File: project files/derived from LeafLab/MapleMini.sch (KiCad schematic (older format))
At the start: 40 parts, among them J1 USB_C, J2 Conn_ST_STDC14, J3 Left, J4 Right, Q1 BC817, Q2 BC817, SW1 Reset, SW2 Button, U1 STM32F103CBTx, U2 MCP1703A-3302_SOT23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

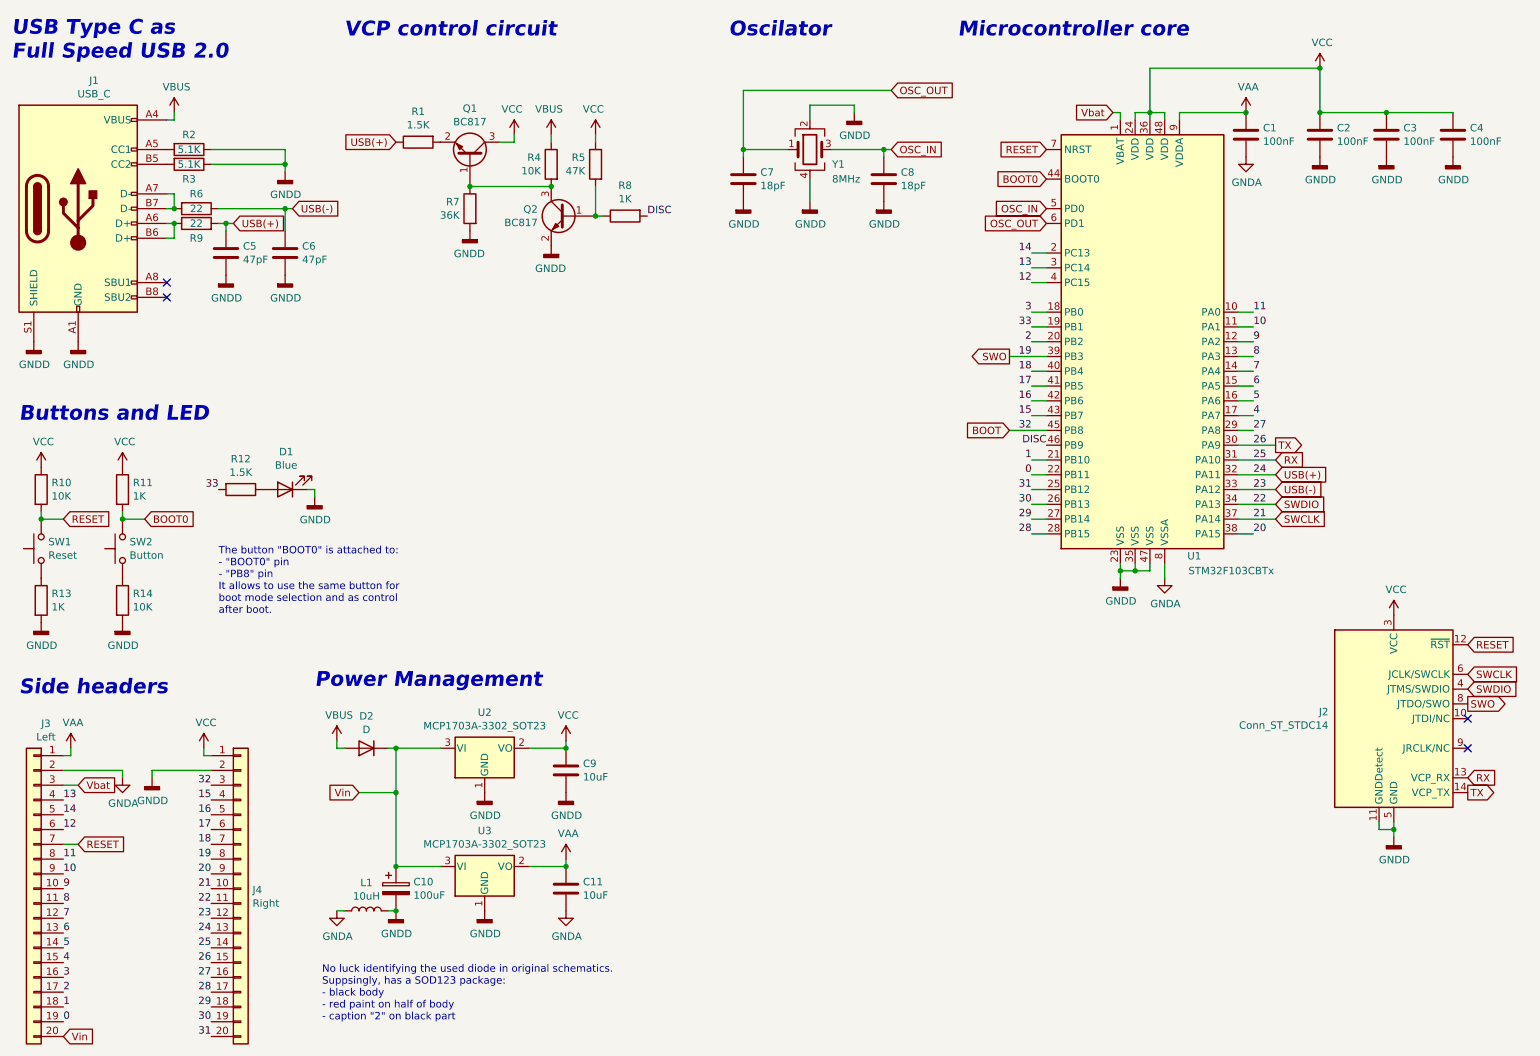
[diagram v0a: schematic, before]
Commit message: power nets renaming
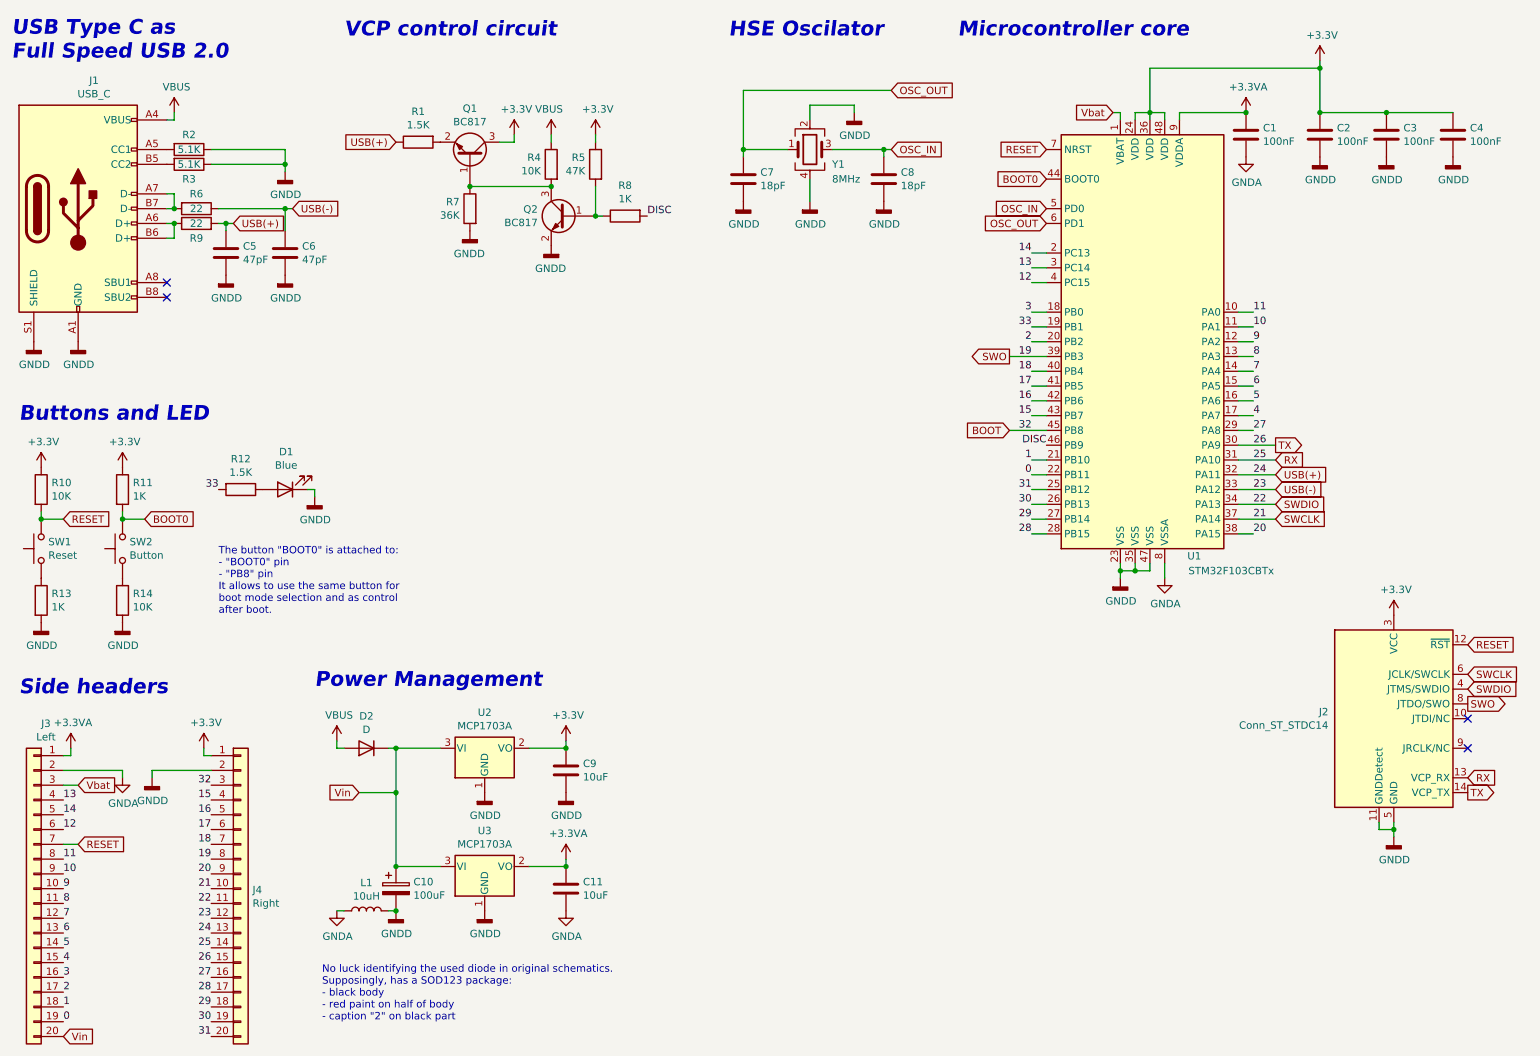
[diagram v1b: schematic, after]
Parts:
- U2, U3: value MCP1703A-3302_SOT23 -> MCP1703A
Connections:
- net VAA renamed +3.3VA
- net VCC renamed +3V3
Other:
- note added: "HSE Oscilator"
- note added: "No luck identifying the used diode in original schematics.\nSupposingly, has a SOD123 package:\n- black body\n- red paint on half of body\n- caption "2" on black part"
- note removed: "No luck identifying the used diode in original schematics.\nSuppsingly, has a SOD123 package:\n- black body\n- red paint on half of body\n- caption "2" on black part"
- note removed: "Oscilator"
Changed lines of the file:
@@
-$EndComp
-$Comp
-L power:VCC #PWR04
-U 1 1 5F576CBF
-P 4100 1500
-F 0 "#PWR04" H 4100 1350 50  0001 C CNN
-F 1 "VCC" H 4115 1673 50  0000 C CNN
-F 2 "" H 4100 1500 50  0001 C CNN
-F 3 "" H 4100 1500 50  0001 C CNN
-	1    4100 1500
-	-1   0    0    -1
 $EndComp
 $Comp
@@
 	-1   0    0    -1
 $EndComp
-$Comp
-L power:VCC #PWR06
-U 1 1 5F588E4C
-P 4650 1500
-F 0 "#PWR06" H 4650 1350 50  0001 C CNN
-F 1 "VCC" H 4665 1673 50  0000 C CNN
-F 2 "" H 4650 1500 50  0001 C CNN
-F 3 "" H 4650 1500 50  0001 C CNN
-	1    4650 1500
-	-1   0    0    -1
-$EndComp
 Wire Wire Line
 	3800 1850 4350 1850
@@
 P 3900 5650
 F 0 "U2" H 3900 5892 50  0000 C CNN
-F 1 "MCP1703A-3302_SOT23" H 3900 5801 50  0000 C CNN
+F 1 "MCP1703A" H 3900 5801 50  0000 C CNN
 F 2 "Package_TO_SOT_SMD:SOT-23" H 3900 5850 50  0001 C CNN
 F 3 "http://ww1.microchip.com/downloads/en/DeviceDoc/20005122B.pdf" H 3900 5600 50  0001 C CNN
@@
 P 3900 6450
 F 0 "U3" H 3900 6692 50  0000 C CNN
-F 1 "MCP1703A-3302_SOT23" H 3900 6601 50  0000 C CNN
+F 1 "MCP1703A" H 3900 6601 50  0000 C CNN
 F 2 "Package_TO_SOT_SMD:SOT-23" H 3900 6650 50  0001 C CNN
 F 3 "http://ww1.microchip.com/downloads/en/DeviceDoc/20005122B.pdf" H 3900 6400 50  0001 C CNN
@@
 $EndComp
 $Comp
-L power:VCC #PWR035
-U 1 1 5F59C36D
-P 4450 5600
-F 0 "#PWR035" H 4450 5450 50  0001 C CNN
-F 1 "VCC" H 4465 5773 50  0000 C CNN
-F 2 "" H 4450 5600 50  0001 C CNN
-F 3 "" H 4450 5600 50  0001 C CNN
-	1    4450 5600
-	1    0    0    -1
-$EndComp
-$Comp
 L power:GNDA #PWR023
 U 1 1 5F59D10D
@@
 F 3 "" H 8500 4500 50  0001 C CNN
 	1    8500 4500
-	1    0    0    -1
-$EndComp
-$Comp
-L power:VAA #PWR039
-U 1 1 5F59E88F
-P 4450 6400
-F 0 "#PWR039" H 4450 6250 50  0001 C CNN
-F 1 "VAA" H 4465 6573 50  0000 C CNN
-F 2 "" H 4450 6400 50  0001 C CNN
-F 3 "" H 4450 6400 50  0001 C CNN
-	1    4450 6400
 	1    0    0    -1
 $EndComp
@@
 $EndComp
 $Comp
-L power:VCC #PWR018
-U 1 1 5F5DF46D
-P 900 3750
-F 0 "#PWR018" H 900 3600 50  0001 C CNN
-F 1 "VCC" H 915 3923 50  0000 C CNN
-F 2 "" H 900 3750 50  0001 C CNN
-F 3 "" H 900 3750 50  0001 C CNN
-	1    900  3750
-	1    0    0    -1
-$EndComp
-$Comp
-L power:VCC #PWR019
-U 1 1 5F5E053F
-P 1450 3750
-F 0 "#PWR019" H 1450 3600 50  0001 C CNN
-F 1 "VCC" H 1465 3923 50  0000 C CNN
-F 2 "" H 1450 3750 50  0001 C CNN
-F 3 "" H 1450 3750 50  0001 C CNN
-	1    1450 3750
-	1    0    0    -1
-$EndComp
-$Comp
 L Device:R R10
 U 1 1 5F5E0C66
@@
 	8600 1350 8600 1400
 $Comp
-L power:VAA #PWR03
-U 1 1 5F61B614
-P 9050 1350
-F 0 "#PWR03" H 9050 1200 50  0001 C CNN
-F 1 "VAA" H 9065 1523 50  0000 C CNN
-F 2 "" H 9050 1350 50  0001 C CNN
-F 3 "" H 9050 1350 50  0001 C CNN
-	1    9050 1350
-	1    0    0    -1
-$EndComp
-Connection ~ 9050 1350
-$Comp
 L power:GNDD #PWR08
 U 1 1 5F61C6D4
@@
 	8400 1050 8400 1350
 Connection ~ 9550 1350
-$Comp
-L power:VCC #PWR01
-U 1 1 5F620163
-P 9550 1050
-F 0 "#PWR01" H 9550 900 50  0001 C CNN
-F 1 "VCC" H 9565 1223 50  0000 C CNN
-F 2 "" H 9550 1050 50  0001 C CNN
-F 3 "" H 9550 1050 50  0001 C CNN
-	1    9550 1050
-	1    0    0    -1
-$EndComp
-Connection ~ 9550 1050
 $Comp
 L Connector_Generic:Conn_01x20 J4
@@
 	1    850  6600
 	-1   0    0    -1
-$EndComp
-$Comp
-L power:VAA #PWR030
-U 1 1 5F62AD2E
-P 1100 5650
-F 0 "#PWR030" H 1100 5500 50  0001 C CNN
-F 1 "VAA" H 1115 5823 50  0000 C CNN
-F 2 "" H 1100 5650 50  0001 C CNN
-F 3 "" H 1100 5650 50  0001 C CNN
-	1    1100 5650
-	1    0    0    -1
 $EndComp
 $Comp
@@
 Wire Wire Line
 	1100 5700 1100 5650
-$Comp
-L power:VCC #PWR031
-U 1 1 5F63C308
-P 2000 5650
-F 0 "#PWR031" H 2000 5500 50  0001 C CNN
-F 1 "VCC" H 2015 5823 50  0000 C CNN
-F 2 "" H 2000 5650 50  0001 C CNN
-F 3 "" H 2000 5650 50  0001 C CNN
-	1    2000 5650
-	1    0    0    -1
-$EndComp
 $Comp
 L power:GNDD #PWR033
@@
 VCP control circuit
 Text Notes 5550 850  0    100  Italic 20
-Oscilator
+HSE Oscilator
 Text Notes 7100 850  0    100  Italic 20
 Microcontroller core
@@
 F 3 "https://www.st.com/content/ccc/resource/technical/document/user_manual/group1/99/49/91/b6/b2/3a/46/e5/DM00526767/files/DM00526767.pdf/jcr:content/translations/en.DM00526767.pdf" V 9700 4200 50  0001 C CNN
 	1    10050 5450
-	1    0    0    -1
-$EndComp
-$Comp
-L power:VCC #PWR027
-U 1 1 5F95D0A5
-P 10050 4750
-F 0 "#PWR027" H 10050 4600 50  0001 C CNN
-F 1 "VCC" H 10065 4923 50  0000 C CNN
-F 2 "" H 10050 4750 50  0001 C CNN
-F 3 "" H 10050 4750 50  0001 C CNN
-	1    10050 4750
 	1    0    0    -1
 $EndComp
@@
 Side headers
 Text Notes 2800 7500 0    50   ~ 0
-No luck identifying the used diode in original schematics.\nSuppsingly, has a SOD123 package:\n- black body\n- red paint on half of body\n- caption "2" on black part
+No luck identifying the used diode in original schematics.\nSupposingly, has a SOD123 package:\n- black body\n- red paint on half of body\n- caption "2" on black part
+$Comp
+L power:+3.3V #PWR?
+U 1 1 5FA4246E
+P 4450 5600
+F 0 "#PWR?" H 4450 5450 50  0001 C CNN
+F 1 "+3.3V" H 4465 5773 50  0000 C CNN
+F 2 "" H 4450 5600 50  0001 C CNN
+F 3 "" H 4450 5600 50  0001 C CNN
+	1    4450 5600
+	1    0    0    -1
+$EndComp
+$Comp
+L power:+3.3VA #PWR?
+U 1 1 5FA42E96
+P 4450 6400
+F 0 "#PWR?" H 4450 6250 50  0001 C CNN
+F 1 "+3.3VA" H 4465 6573 50  0000 C CNN
+F 2 "" H 4450 6400 50  0001 C CNN
+F 3 "" H 4450 6400 50  0001 C CNN
+	1    4450 6400
+	1    0    0    -1
+$EndComp
+$Comp
+L power:+3.3VA #PWR?
+U 1 1 5FA441A2
+P 9050 1350
+F 0 "#PWR?" H 9050 1200 50  0001 C CNN
+F 1 "+3.3VA" H 9065 1523 50  0000 C CNN
+F 2 "" H 9050 1350 50  0001 C CNN
+F 3 "" H 9050 1350 50  0001 C CNN
+	1    9050 1350
+	1    0    0    -1
+$EndComp
+Connection ~ 9050 1350
+$Comp
+L power:+3.3VA #PWR?
+U 1 1 5FA45E5F
+P 1100 5650
+F 0 "#PWR?" H 1100 5500 50  0001 C CNN
+F 1 "+3.3VA" H 1115 5823 50  0000 C CNN
+F 2 "" H 1100 5650 50  0001 C CNN
+F 3 "" H 1100 5650 50  0001 C CNN
+	1    1100 5650
+	1    0    0    -1
+$EndComp
+$Comp
+L power:+3.3V #PWR?
+U 1 1 5FA466DA
+P 2000 5650
+F 0 "#PWR?" H 2000 5500 50  0001 C CNN
+F 1 "+3.3V" H 2015 5823 50  0000 C CNN
+F 2 "" H 2000 5650 50  0001 C CNN
+F 3 "" H 2000 5650 50  0001 C CNN
+	1    2000 5650
+	1    0    0    -1
+$EndComp
+$Comp
+L power:+3.3V #PWR?
+U 1 1 5FA4713F
+P 10050 4750
+F 0 "#PWR?" H 10050 4600 50  0001 C CNN
+F 1 "+3.3V" H 10065 4923 50  0000 C CNN
+F 2 "" H 10050 4750 50  0001 C CNN
+F 3 "" H 10050 4750 50  0001 C CNN
+	1    10050 4750
+	1    0    0    -1
+$EndComp
+$Comp
+L power:+3.3V #PWR?
+U 1 1 5FA4799E
+P 9550 1000
+F 0 "#PWR?" H 9550 850 50  0001 C CNN
+F 1 "+3.3V" H 9565 1173 50  0000 C CNN
+F 2 "" H 9550 1000 50  0001 C CNN
+F 3 "" H 9550 1000 50  0001 C CNN
+	1    9550 1000
+	1    0    0    -1
+$EndComp
+Wire Wire Line
+	9550 1000 9550 1050
+Connection ~ 9550 1050
+$Comp
+L power:+3.3V #PWR?
+U 1 1 5FA4D0BA
+P 4650 1500
+F 0 "#PWR?" H 4650 1350 50  0001 C CNN
+F 1 "+3.3V" H 4665 1673 50  0000 C CNN
+F 2 "" H 4650 1500 50  0001 C CNN
+F 3 "" H 4650 1500 50  0001 C CNN
+	1    4650 1500
+	1    0    0    -1
+$EndComp
+$Comp
+L power:+3.3V #PWR?
+U 1 1 5FA4DA8B
+P 4100 1500
+F 0 "#PWR?" H 4100 1350 50  0001 C CNN
+F 1 "+3.3V" H 4115 1673 50  0000 C CNN
+F 2 "" H 4100 1500 50  0001 C CNN
+F 3 "" H 4100 1500 50  0001 C CNN
+	1    4100 1500
+	1    0    0    -1
+$EndComp
+$Comp
+L power:+3.3V #PWR?
+U 1 1 5FA4E235
+P 1450 3750
+F 0 "#PWR?" H 1450 3600 50  0001 C CNN
+F 1 "+3.3V" H 1465 3923 50  0000 C CNN
+F 2 "" H 1450 3750 50  0001 C CNN
+F 3 "" H 1450 3750 50  0001 C CNN
+	1    1450 3750
+	1    0    0    -1
+$EndComp
+$Comp
+L power:+3.3V #PWR?
+U 1 1 5FA4EF95
+P 900 3750
+F 0 "#PWR?" H 900 3600 50  0001 C CNN
+F 1 "+3.3V" H 915 3923 50  0000 C CNN
+F 2 "" H 900 3750 50  0001 C CNN
+F 3 "" H 900 3750 50  0001 C CNN
+	1    900  3750
+	1    0    0    -1
+$EndComp
 $EndSCHEMATC

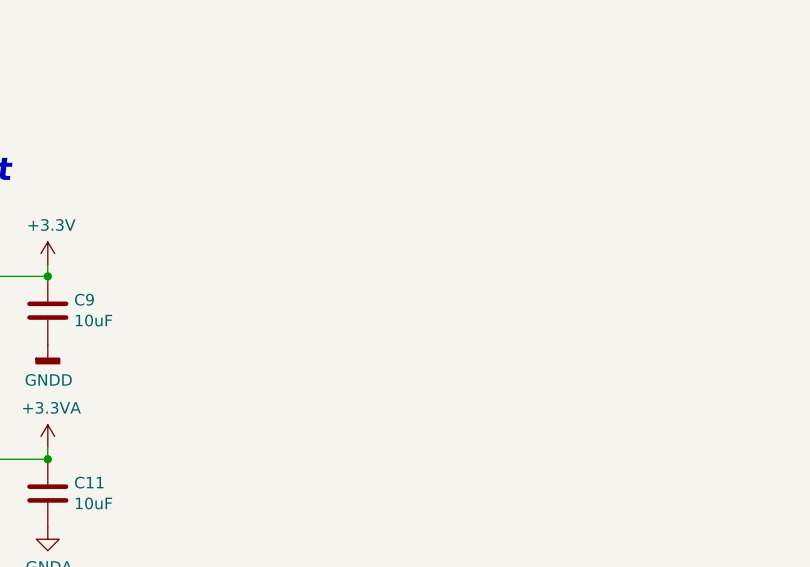
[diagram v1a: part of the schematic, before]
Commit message: added extra references
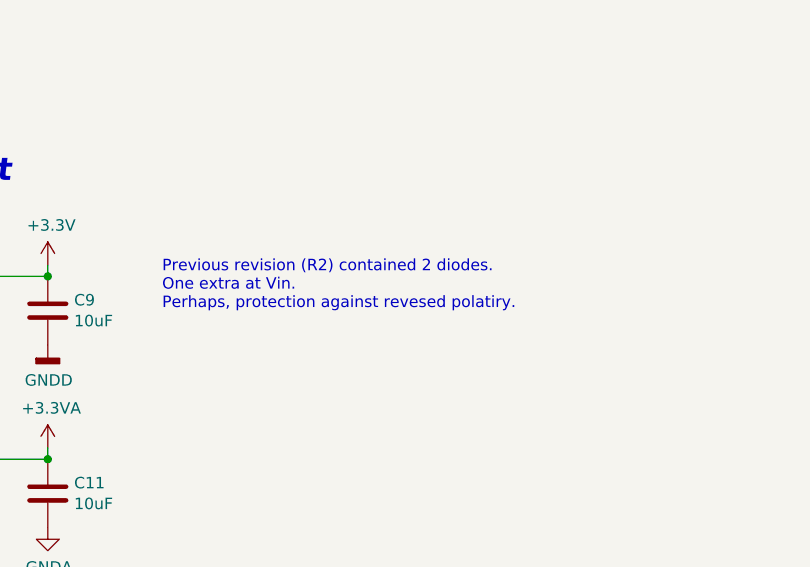
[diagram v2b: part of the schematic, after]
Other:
- note added: "Previous revision (R2) contained 2 diodes.\nOne extra at Vin.\nPerhaps, protection against revesed polatiry."
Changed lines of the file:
@@
 	1    0    0    -1
 $EndComp
+Text Notes 4950 5800 0    50   ~ 0
+Previous revision (R2) contained 2 diodes.\nOne extra at Vin.\nPerhaps, protection against revesed polatiry.
 $EndSCHEMATC
